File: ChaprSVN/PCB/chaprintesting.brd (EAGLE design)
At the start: 68.6 x 55.6 mm, 30 parts, among them M2 RN42 Module, T1 3906, T2 3904

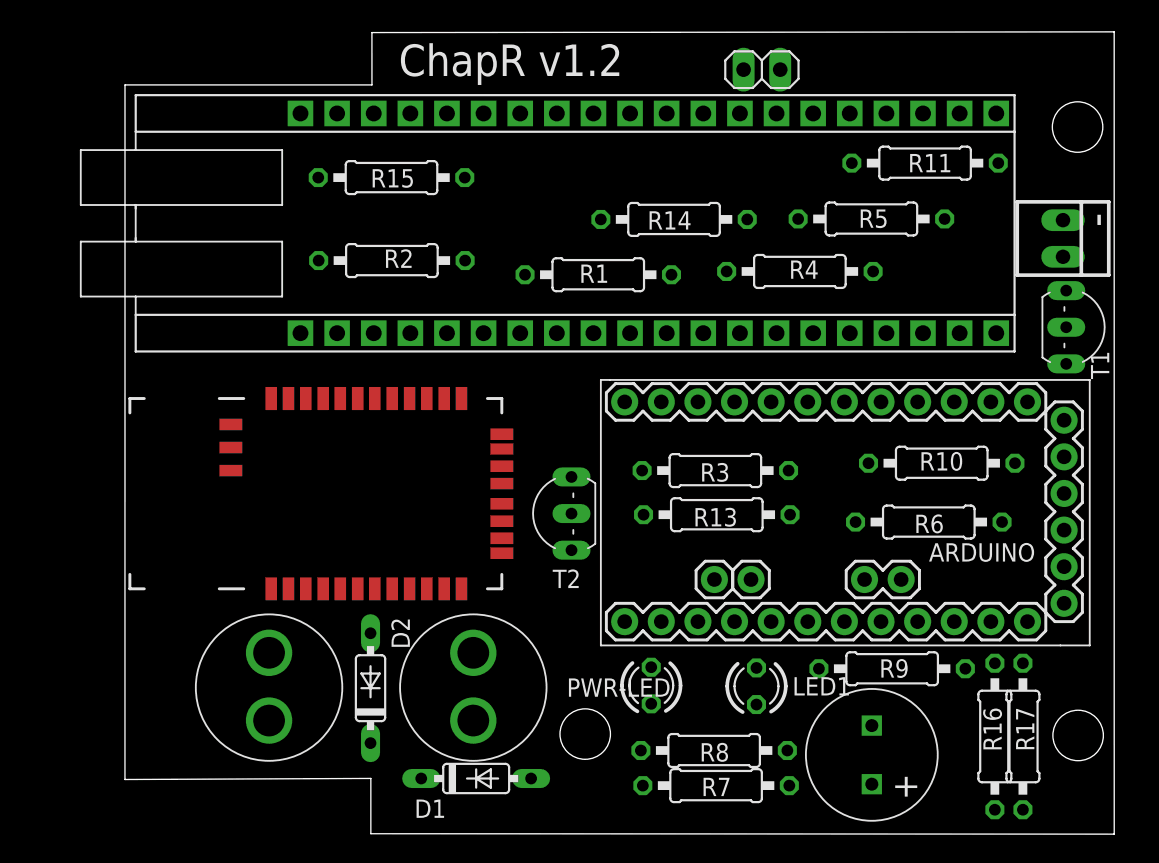
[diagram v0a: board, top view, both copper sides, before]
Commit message: 
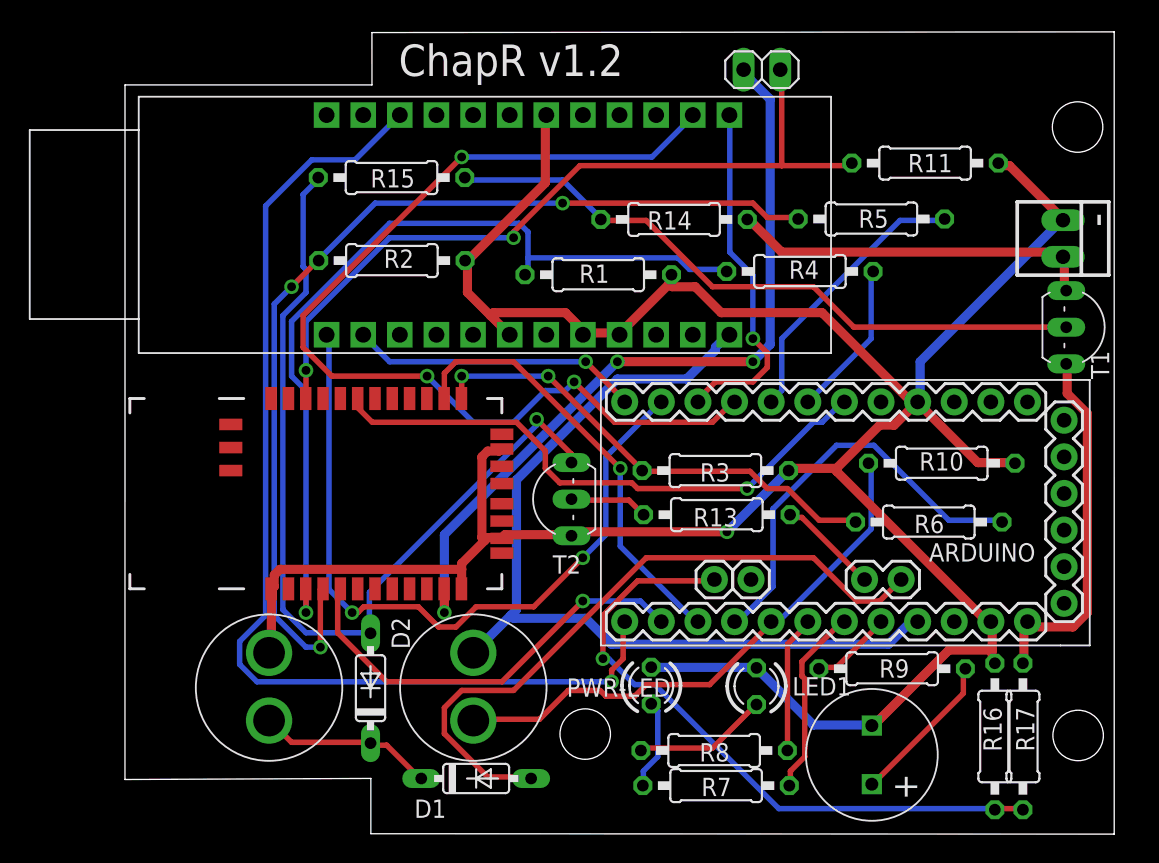
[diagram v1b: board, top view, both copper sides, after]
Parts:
- removed U$3: VDIP2BIGHOLE, ChapR-Custom:VDIP2-BIGHOLE
- added U$1: V2DIP2, ChapR-Custom:V2DIP2
- moved T2 1.00 mm to (31.7, 23.9)
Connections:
- removed net LED1(BD5): U$3.4
- removed net LED2(BD6): U$3.5
- removed net NC(1): U$3.1
- removed net NC(2): U$3.40
- new net N$28: U$1.P$24
- net +3V3: no longer U$3.32, U$3.38, U$3.39
- net +5V: now also U$1.P$1; no longer U$3.2, U$3.3, U$3.9
- net GND: now also U$1.P$18, U$1.P$4, U$1.P$5, U$1.P$7; no longer U$3.12, U$3.13, U$3.15, U$3.26
- net N$10: now also ARDUINO.D6, U$1.P$14; no longer ARDUINO.D9, U$3.18
- net N$11: now also ARDUINO.D7, U$1.P$13; no longer ARDUINO.D8, U$3.17
- net N$12: now also ARDUINO.D8, U$1.P$12; no longer ARDUINO.D7, U$3.16
- net N$13: now also ARDUINO.D9, U$1.P$11; no longer ARDUINO.D6, U$3.14
- net N$2: now also U$1.P$22; no longer U$3.30
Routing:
- net GND: track 0.00 -> 196.9 mm, vias 0 -> 1
- net N$2: track 0.00 -> 75.3 mm, vias 0 -> 1
- net N$10: track 0.00 -> 70.0 mm, vias 0 -> 3
- net N$7: track 0.00 -> 69.6 mm, vias 0 -> 3
- net +5V: track 0.00 -> 62.1 mm
- net N$25: track 0.00 -> 61.5 mm, vias 0 -> 1
- net N$6: track 0.00 -> 58.9 mm, vias 0 -> 1
- net +3V3: track 0.00 -> 55.1 mm, vias 0 -> 3
- net N$22: track 0.00 -> 54.8 mm, vias 0 -> 2
- net N$12: track 0.00 -> 51.9 mm, vias 0 -> 2
- net N$29: track 0.00 -> 47.0 mm
- net N$1: track 0.00 -> 46.0 mm
- net N$31: track 0.00 -> 45.3 mm, vias 0 -> 1
- net N$15: track 0.00 -> 39.9 mm, vias 0 -> 1
- net N$24: track 0.00 -> 38.1 mm
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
